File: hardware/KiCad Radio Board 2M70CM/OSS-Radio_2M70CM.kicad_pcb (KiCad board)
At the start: 4 copper layers, 32 x 40.5 mm, 110 parts, among them J1 DF40C-24DP-0.4V, Q1 BSS138, Q2 BSS138, Q3 BSS138, U3 GRF5504, U4 TPS7A4701xRGW, U5 CC1200, U6 AT24CS01-STUM, U7 SKY13330-397LF, Y4 TG-5021CG

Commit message: changed mounting holes on 2M70CM board
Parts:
- removed TP4: TestPoint, TestPoint:TestPoint_Pad_D1.0mm
- moved MP2 1.75 mm to (156.5, 83.0)
- moved H1 1.41 mm to (162.5, 83.0)
- moved H2 1.41 mm to (137.5, 83.0)
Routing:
- net GND: track 64.1 -> 71.2 mm, vias 196 -> 191
- net 5V_RF: track 8.84 -> 10.6 mm
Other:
- board size 32 x 40.5 mm -> 31 x 40 mm

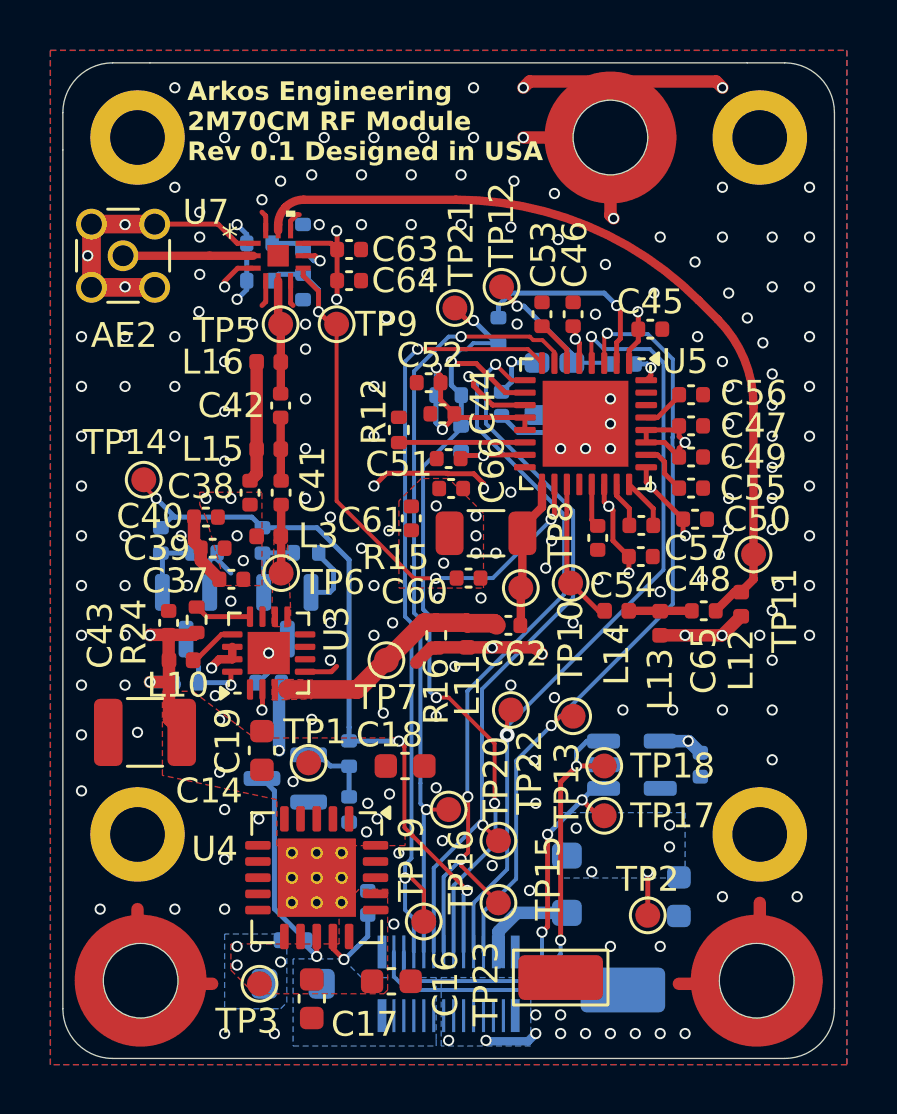
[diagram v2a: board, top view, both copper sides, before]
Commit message: Rev 0.2, added 0 ohm resistor on GPIO0, fixed some DRC errors and added optional pogo pin power interface if needed
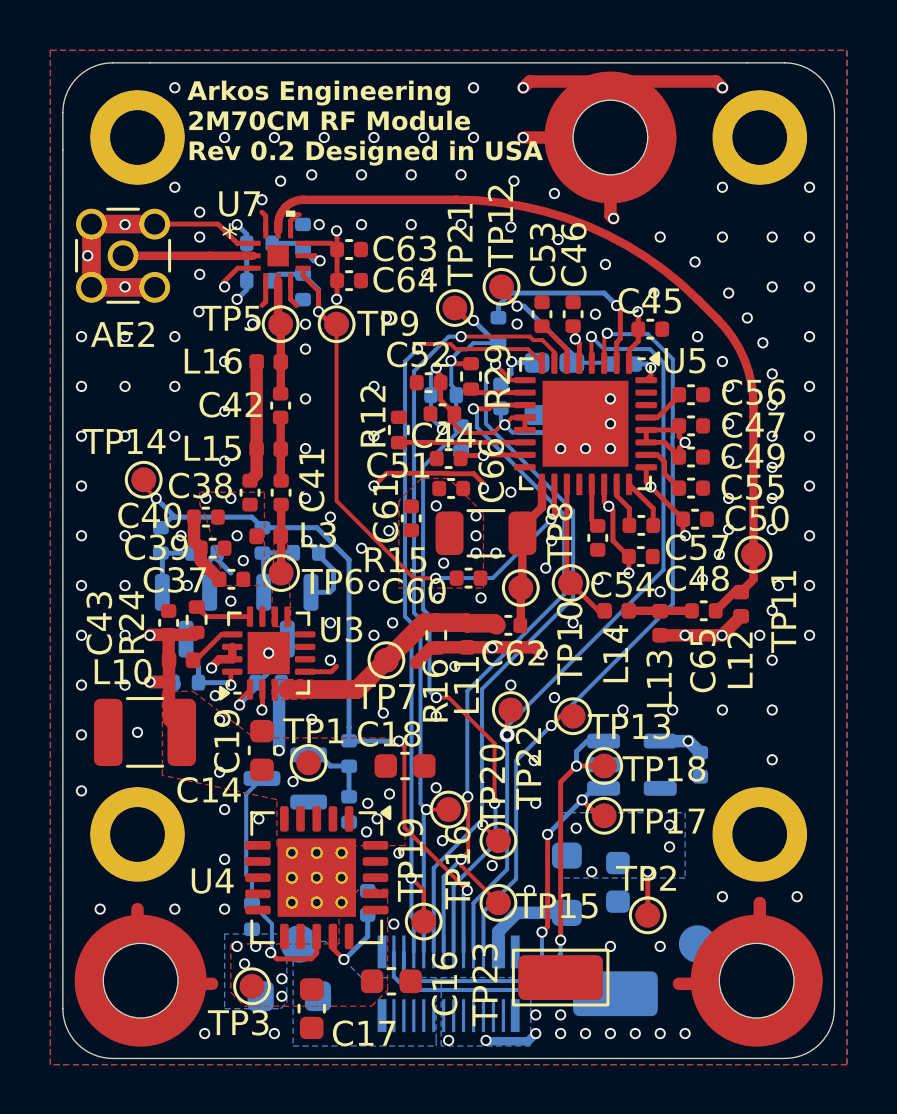
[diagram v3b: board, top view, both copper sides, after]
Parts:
- added J2: P70-7000045, TestPoint:TestPoint_Pad_D1.5mm, B.Cu at (144.0, 115.4)
- added J3: P70-7000045, TestPoint:TestPoint_Pad_D1.5mm, B.Cu at (160.0, 115.4)
- added R29: 0, Resistor_SMD:R_0402_1005Metric, F.Cu at (150.9, 92.6)
- moved C23 2.52 mm to (156.8, 112.9)
- moved R26 1.90 mm to (142.1, 114.3), turned to 90 degrees
- moved FB2 0.52 mm to (143.6, 117.5)
- moved C17 0.40 mm to (144.5, 118.0)
- moved TP24 0.34 mm to (156.7, 117.4)
- moved TP3 0.32 mm to (142.1, 117.1)
- moved C59 0.30 mm to (152.1, 93.4)
- moved R13 0.20 mm to (149.8, 93.3)
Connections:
- U5 pad 10: RF_GPIO0 -> Net-(U5-GPIO0)
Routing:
- net RF_GPIO0: track 34.7 -> 32.2 mm
- net Net-(U5-GPIO0): track 0.00 -> 2.22 mm
- net RF_SEL: track 31.9 -> 29.9 mm
- net Net-(Q1-D): track 2.33 -> 4.30 mm, vias 0 -> 1
- net 3V3: track 42.0 -> 43.8 mm, vias 25 -> 26
- net ENABLE_5V_RF: track 8.86 -> 10.3 mm
- net V_BAT: track 0.00 -> 0.85 mm, vias 4 -> 5
- net GND: track 71.2 -> 71.6 mm, vias 191 -> 192
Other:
- board text added: "Arkos Engineering 2M70CM RF Module Rev 0.2 Designed in USA"
- board text removed: "Arkos Engineering 2M70CM RF Module Rev 0.1 Designed in USA"

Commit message: fixed pogo foorprints and did rev 0.2 exports
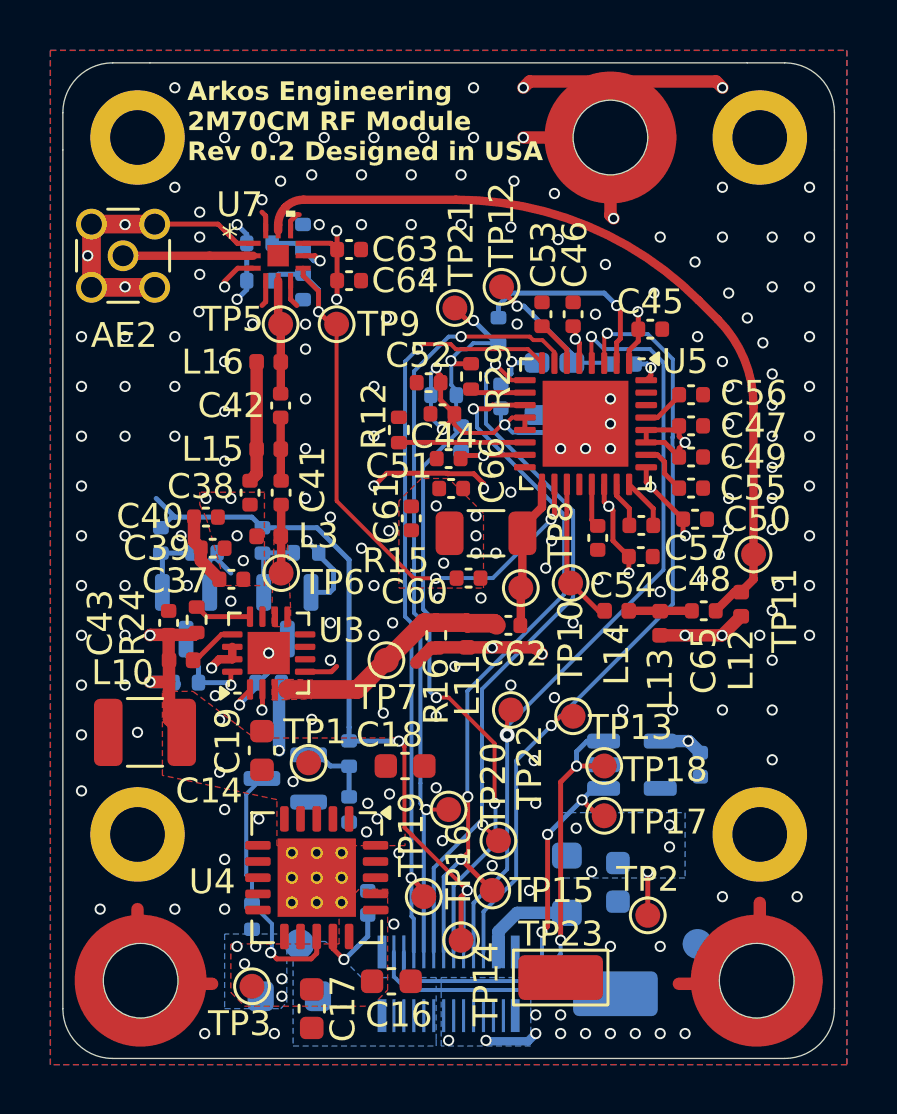
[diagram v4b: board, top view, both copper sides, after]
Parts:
- moved TP14 22.5 mm to (150.5, 115.2)
- moved TP19 1.00 mm to (149.0, 113.5)
- moved TP15 0.56 mm to (151.8, 113.2)
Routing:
- net RF_GPIO1: track 29.3 -> 30.6 mm, vias 3 -> 2
- net RF_SCLK: track 31.9 -> 30.9 mm
- net RF_SEL: track 29.9 -> 29.3 mm
